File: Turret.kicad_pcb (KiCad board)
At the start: 2 copper layers, 104 x 54 mm, 25 parts, among them J1 Conn_01x04_Pin, J10 Conn_01x02_Pin, J12 Conn_01x02_Pin, J13 Conn_01x04_Pin, J14 Conn_01x04_Pin, J15 Conn_01x08_Pin, J2 Conn_01x02_Pin, J20 Conn_01x02_Pin, J21 Conn_01x02_Pin, J3 Conn_01x02_Pin, J4 Conn_01x02_Pin, J5 Conn_01x04_Pin, J6 Conn_01x02_Pin, J7 Conn_01x02_Pin, J8 Conn_01x02_Pin, J9 Conn_01x02_Pin

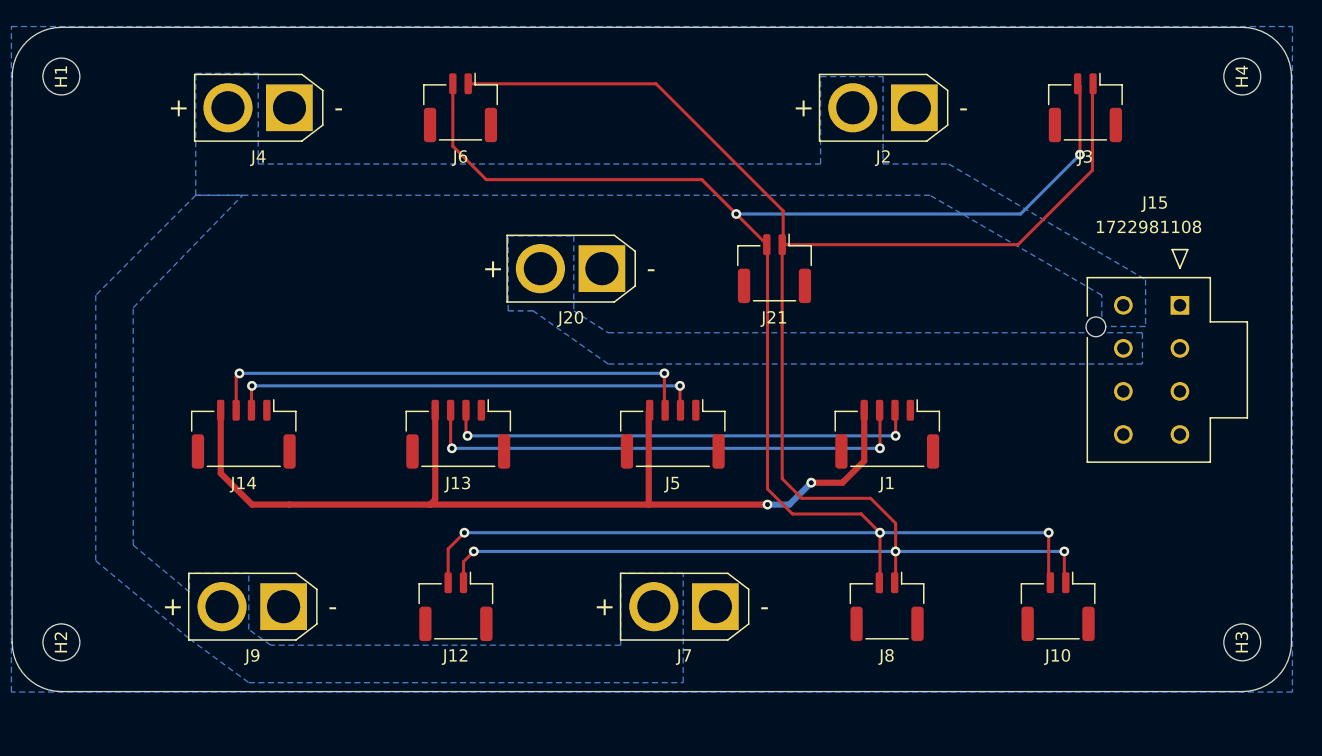
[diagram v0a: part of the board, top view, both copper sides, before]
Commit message: Adding new ref system, other push now deprecated
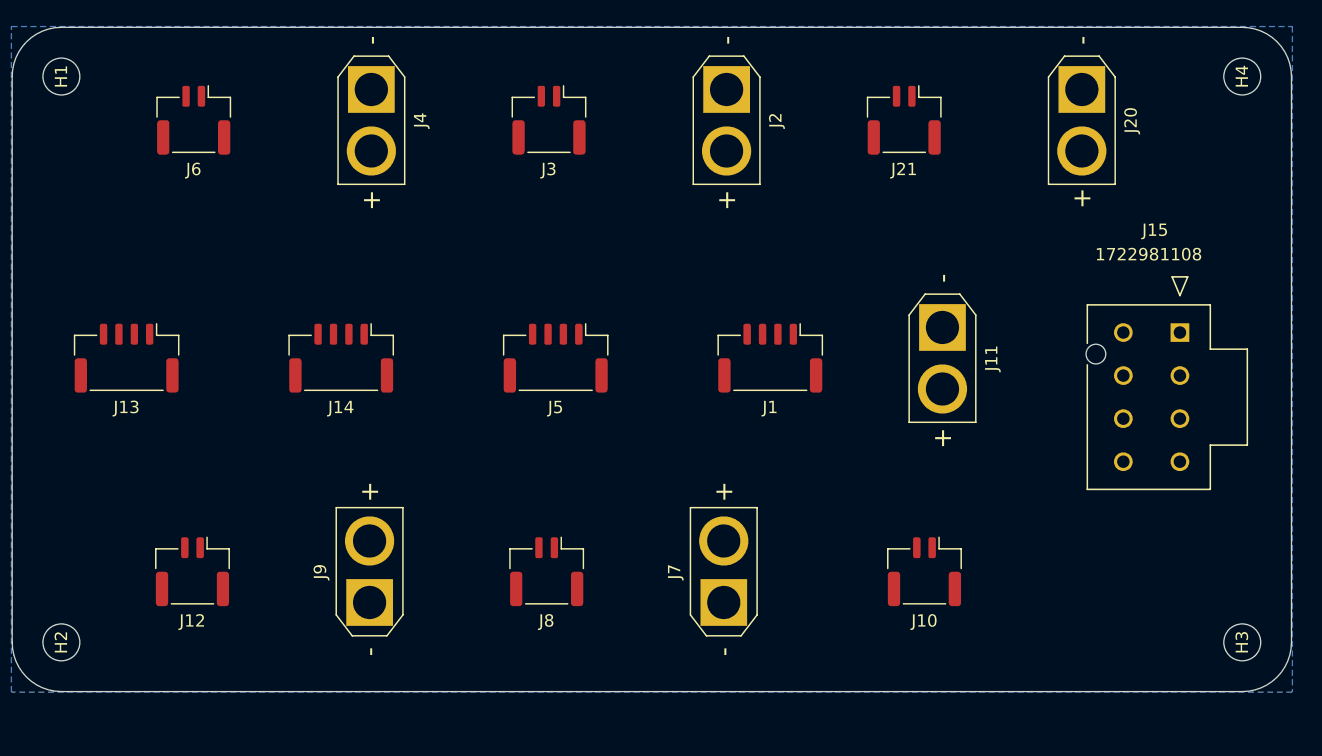
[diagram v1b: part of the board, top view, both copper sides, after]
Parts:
- added J11: Conn_01x02_Pin, Connector_AMASS:AMASS_XT30U-F_1x02_P5.0mm_Vertical, F.Cu at (116.1, 58.5)
- moved J3 43.6 mm to (84.1, 41.7)
- moved J20 41.6 mm to (127.4, 39.2), turned to -90 degrees
- moved J8 27.8 mm to (83.9, 78.4)
- moved J13 27.7 mm to (49.8, 61.0)
- moved J6 21.7 mm to (55.2, 41.7)
- moved J12 21.6 mm to (55.1, 78.4)
- moved J21 16.0 mm to (113.0, 41.7)
- moved J2 15.3 mm to (98.5, 39.2), turned to -90 degrees
- moved J5 11.3 mm to (84.6, 61.0)
- moved J1 11.3 mm to (102.1, 61.0)
- moved J10 11.2 mm to (114.6, 78.4)
- moved J14 10.0 mm to (67.2, 61.0)
- moved J9 7.00 mm to (69.5, 80.9), turned to 90 degrees
- moved J4 6.82 mm to (69.6, 39.2), turned to -90 degrees
- moved J15 2.21 mm to (135.4, 58.9)
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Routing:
- net /CANH: track 160.5 -> 0.00 mm, vias 5 -> 0
- net /CANL: track 155.5 -> 0.00 mm, vias 3 -> 0
- net +3.3V: track 79.6 -> 0.00 mm, vias 2 -> 0
- net /UART_RX: track 41.0 -> 0.00 mm, vias 2 -> 0
- net /SWCLK: track 40.7 -> 0.00 mm, vias 2 -> 0
- net /UART_TX: track 39.0 -> 0.00 mm, vias 2 -> 0
- net /SWDIO: track 38.8 -> 0.00 mm, vias 2 -> 0
- removed copper zone on B.Cu, net /+24V_Gimbal
- removed copper zone on B.Cu, net /+24V_Shooter

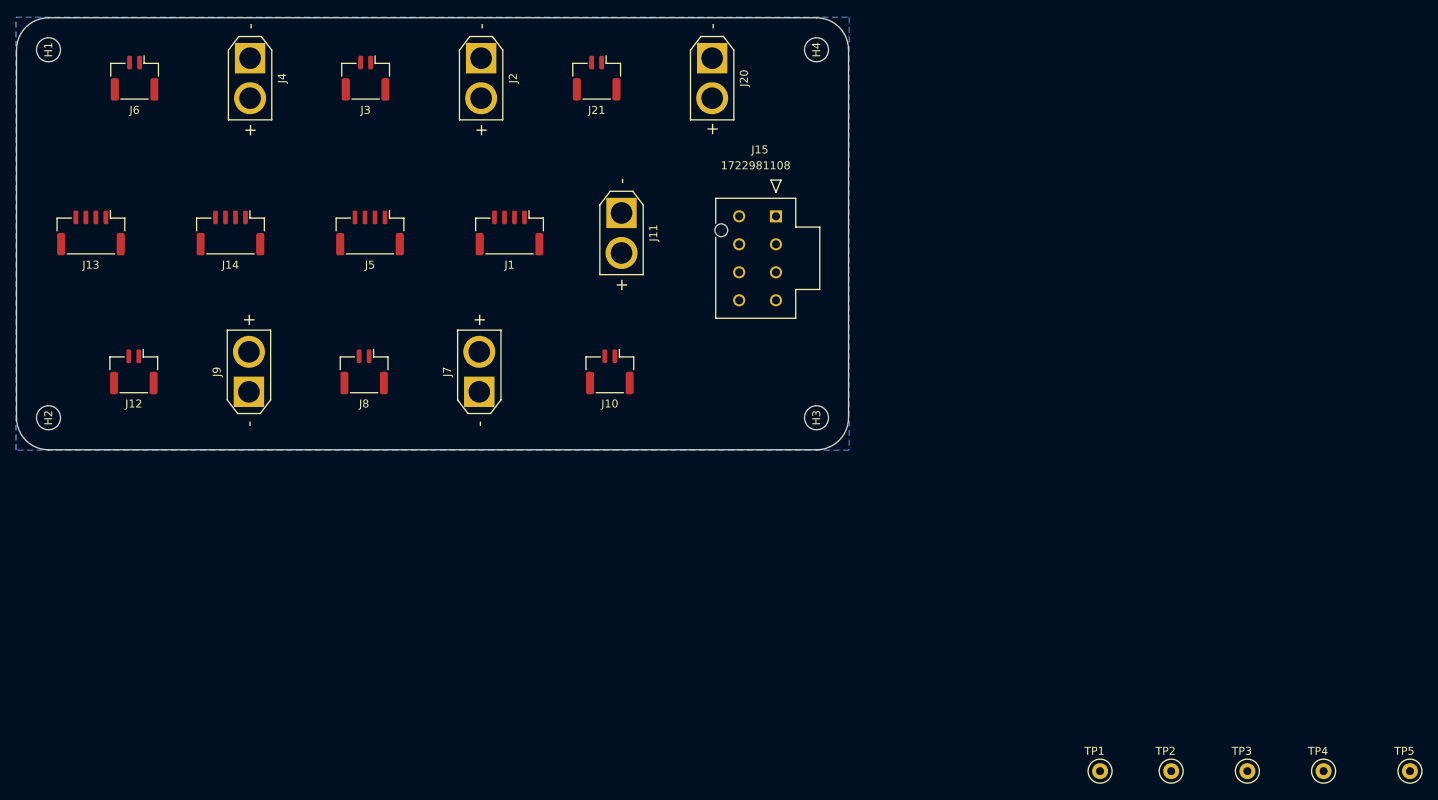
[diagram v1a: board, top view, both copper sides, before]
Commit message: New layout, test points not final
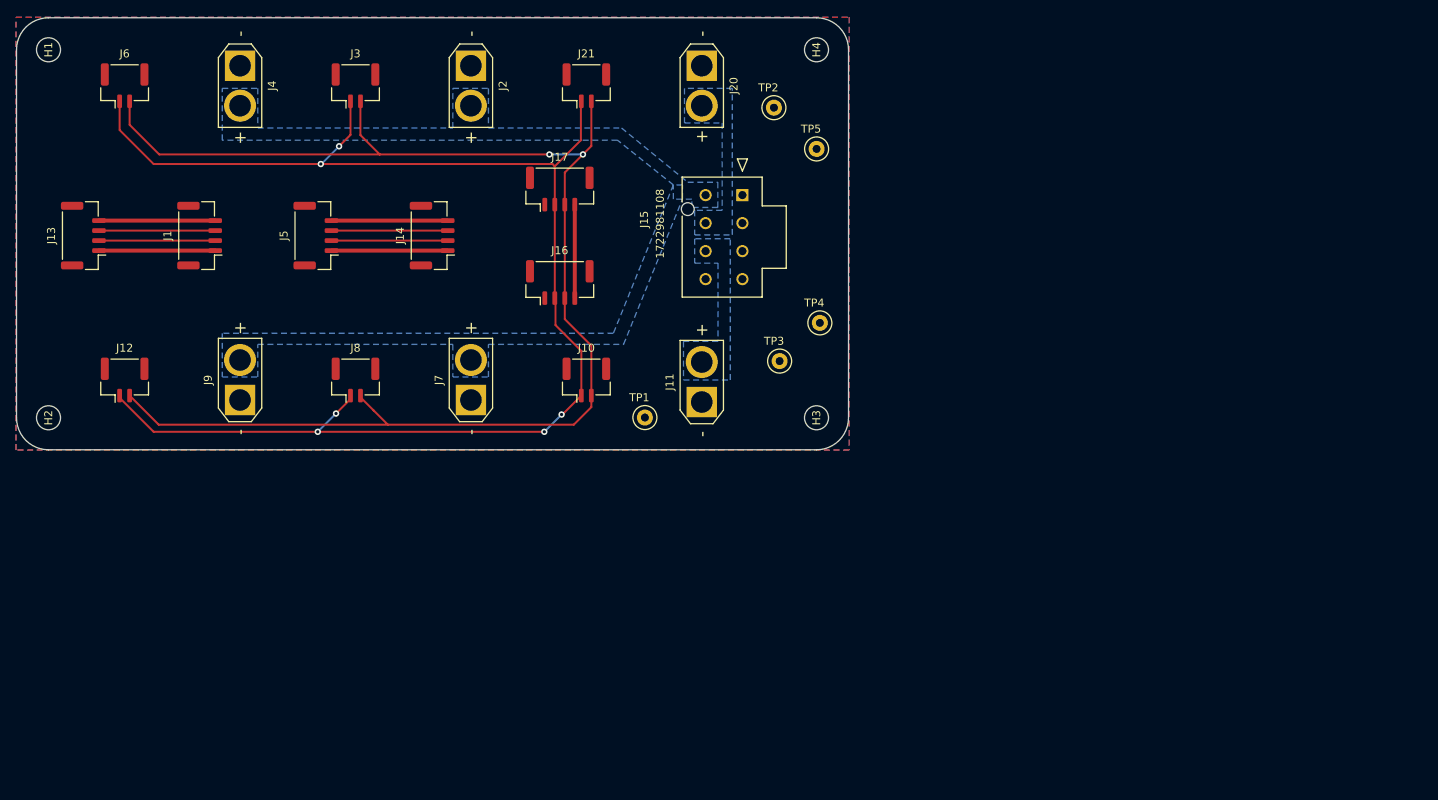
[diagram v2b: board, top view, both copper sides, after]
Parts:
- added J16: Conn_01x04_Pin, Connector_JST:JST_GH_BM04B-GHS-TBT_1x04-1MP_P1.25mm_Vertical, F.Cu at (108.4, 67.2)
- added J17: Conn_01x04_Pin, Connector_JST:JST_GH_BM04B-GHS-TBT_1x04-1MP_P1.25mm_Vertical, F.Cu at (108.4, 55.5)
- moved TP5 107.5 mm to (140.5, 50.5)
- moved TP2 96.7 mm to (135.1, 45.3)
- moved TP4 84.3 mm to (140.9, 72.2)
- moved TP3 77.8 mm to (135.8, 77.0)
- moved TP1 72.0 mm to (119.0, 84.1)
- moved J1 38.7 mm to (63.3, 61.3), turned to 90 degrees
- moved J11 25.7 mm to (126.1, 82.1), turned to 90 degrees
- moved J14 25.2 mm to (92.4, 61.3), turned to 90 degrees
- moved J5 6.77 mm to (77.9, 61.3), turned to 90 degrees
- moved J15 4.96 mm to (131.2, 56.3)
- moved J10 3.11 mm to (111.7, 79.4), turned to 0 degrees
- moved J20 1.60 mm to (126.1, 40.1)
- moved J21 1.59 mm to (111.7, 42.6), turned to 0 degrees
- moved J2 1.58 mm to (97.3, 40.1)
- moved J3 1.58 mm to (82.8, 42.6), turned to 0 degrees
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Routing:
- net /CANL: track 0.00 -> 176.7 mm, vias 0 -> 6
- net /CANH: track 0.00 -> 174.9 mm, vias 0 -> 2
- net GND: track 0.00 -> 29.1 mm
- net +3.3V: track 0.00 -> 29.1 mm
- net /UART_TX: track 0.00 -> 14.5 mm
- net /UART_RX: track 0.00 -> 14.5 mm
- net /SWDIO: track 0.00 -> 14.5 mm
- net /SWCLK: track 0.00 -> 14.5 mm
- net /Ref_PWR: track 0.00 -> 11.7 mm
- added copper zone on B.Cu, net /+19V
- added copper zone on B.Cu, net /+24V_Gimbal
- added copper zone on B.Cu, net /+24V_Shooter
- added copper zone on F.Cu, net GND

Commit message: Added connections to test points, silkscreens need to be renamed.
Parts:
- moved TP3 7.41 mm to (134.0, 84.2)
- moved TP2 7.33 mm to (134.0, 38.1)
- moved TP4 0.43 mm to (140.4, 72.3)
- moved TP5 0.15 mm to (140.4, 50.3)
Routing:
- net /+5V: track 0.00 -> 16.2 mm
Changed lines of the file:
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@@
   )
   (footprint "TestPoint:TestPoint_Loop_D1.80mm_Drill1.0mm_Beaded" (layer "F.Cu")
-    (at 135.128 45.339 180)
+    (at 133.9596 38.1 180)
     (descr "wire loop with bead as test point, loop diameter 1.8mm, hole diameter 1.0mm")
     (tags "test point wire loop bead")
@@
   )
   (footprint "TestPoint:TestPoint_Loop_D1.80mm_Drill1.0mm_Beaded" (layer "F.Cu")
-    (at 135.8392 77.0128 180)
+    (at 133.9596 84.1756 180)
     (descr "wire loop with bead as test point, loop diameter 1.8mm, hole diameter 1.0mm")
     (tags "test point wire loop bead")
@@
   )
   (footprint "TestPoint:TestPoint_Loop_D1.80mm_Drill1.0mm_Beaded" (layer "F.Cu")
-    (at 140.8684 72.2376 180)
+    (at 140.45 72.3392 180)
     (descr "wire loop with bead as test point, loop diameter 1.8mm, hole diameter 1.0mm")
     (tags "test point wire loop bead")
@@
   )
   (footprint "TestPoint:TestPoint_Loop_D1.80mm_Drill1.0mm_Beaded" (layer "F.Cu")
-    (at 140.462 50.4952 180)
+    (at 140.45 50.3428 180)
     (descr "wire loop with bead as test point, loop diameter 1.8mm, hole diameter 1.0mm")
     (tags "test point wire loop bead")
@@
   (segment (start 79.820334 61.953) (end 94.354167 61.953) (width 0.25) (layer "F.Cu") (net 7))
   (segment (start 79.820334 60.703) (end 94.354167 60.703) (width 0.25) (layer "F.Cu") (net 8))
+  (segment (start 126.587999 66.766002) (end 132.161197 72.3392) (width 0.25) (layer "F.Cu") (net 12))
+  (segment (start 132.161197 72.3392) (end 140.45 72.3392) (width 0.25) (layer "F.Cu") (net 12))
   (segment (start 110.233 57.457) (end 110.233 69.141) (width 0.5) (layer "F.Cu") (net 13))
   (zone (net 3) (net_name "GND") (layer "F.Cu") (hatch edge 0.5)
@@
       (pts
         (xy 128.1176 54.6608)
-        (xy 128.1176 57.8104)
-        (xy 124.8664 57.8104)
+        (xy 128.1176 57.6326)
+        (xy 124.8664 57.6326)
         (xy 124.8664 56.769)
         (xy 122.555 56.769)
@@
     )
   )
+  (zone (net 10) (net_name "/+24V_Gimbal") (layer "B.Cu") (hatch edge 0.5)
+    (priority 7)
+    (connect_pads (clearance 0.5))
+    (min_thickness 0.25) (filled_areas_thickness no)
+    (fill yes (thermal_gap 0.5) (thermal_bridge_width 0.5))
+    (polygon
+      (pts
+        (xy 129.921 43.5102)
+        (xy 129.921 42.926)
+        (xy 129.3876 42.926)
+        (xy 132.1308 39.3954)
+        (xy 132.1308 36.2458)
+        (xy 135.7884 36.2712)
+        (xy 135.7884 39.9288)
+        (xy 132.6388 39.9288)
+      )
+    )
+  )
+  (zone (net 11) (net_name "/+19V") (layer "B.Cu") (hatch edge 0.5)
+    (priority 6)
+    (connect_pads (clearance 0.5))
+    (min_thickness 0.25) (filled_areas_thickness no)
+    (fill yes (thermal_gap 0.5) (thermal_bridge_width 0.5))
+    (polygon
+      (pts
+        (xy 129.667 79.375)
+        (xy 132.1308 82.3976)
+        (xy 132.1308 86.0044)
+        (xy 135.7892 86.0044)
+        (xy 135.7892 82.3484)
+        (xy 133.05 82.3484)
+        (xy 129.667 78.2)
+      )
+    )
+  )
+  (zone (net 9) (net_name "/+24V_Shooter") (layer "B.Cu") (hatch edge 0.5)
+    (priority 5)
+    (connect_pads (clearance 0.5))
+    (min_thickness 0.25) (filled_areas_thickness no)
+    (fill yes (thermal_gap 0.5) (thermal_bridge_width 0.5))
+    (polygon
+      (pts
+        (xy 116.8146 73.7362)
+        (xy 116.332 74.93)
+        (xy 118.364 80.518)
+        (xy 118.364 82.2452)
+        (xy 117.1448 82.2452)
+        (xy 117.1956 85.9028)
+        (xy 120.8532 85.9028)
+        (xy 120.8532 82.2452)
+        (xy 119.2022 82.2452)
+        (xy 119.2022 80.518)
+      )
+    )
+  )
   (zone (net 11) (net_name "/+19V") (layer "B.Cu") (hatch edge 0.5)
     (priority 1)
@@
         (xy 123.825 74.549)
         (xy 123.825 79.375)
-        (xy 129.667 79.375)
-        (xy 129.667 61.722)
+        (xy 129.921 79.375)
+        (xy 129.921 61.722)
       )
     )

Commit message: Tried to fix footprints, also changed to traces for testpoints
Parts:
- +19V_Turret->Orin1: renamed from J11; footprint Connector_AMASS:AMASS_XT30U-F_1x02_P5.0mm_Vertical -> Robomaster_ICs:AMASS_XT30U-F_1x02_P5.0mm_Vertical_copy
- +24V_Feeder1: renamed from J7; footprint Connector_AMASS:AMASS_XT30U-F_1x02_P5.0mm_Vertical -> Robomaster_ICs:AMASS_XT30U-F_1x02_P5.0mm_Vertical_copy
- +24V_Gimbal1: renamed from J20; footprint Connector_AMASS:AMASS_XT30U-F_1x02_P5.0mm_Vertical -> Robomaster_ICs:AMASS_XT30U-F_1x02_P5.0mm_Vertical_copy
- +24V_L_Flywheel1: renamed from J2; footprint Connector_AMASS:AMASS_XT30U-F_1x02_P5.0mm_Vertical -> Robomaster_ICs:AMASS_XT30U-F_1x02_P5.0mm_Vertical_copy
- +24V_R_Flywheel1: renamed from J4; footprint Connector_AMASS:AMASS_XT30U-F_1x02_P5.0mm_Vertical -> Robomaster_ICs:AMASS_XT30U-F_1x02_P5.0mm_Vertical_copy
- +24V_Waterwheel1: renamed from J9; footprint Connector_AMASS:AMASS_XT30U-F_1x02_P5.0mm_Vertical -> Robomaster_ICs:AMASS_XT30U-F_1x02_P5.0mm_Vertical_copy
- renumbered TP3 to +19V1, TP2 to +24V_Gimbal2, TP1 to +24V_Shooter2, TP4 to +5V1, J15 to 8_Pin_Slipring->Turret1, J8 to CAN_Feeder1, J21 to CAN_Gimbal1, J10 to CAN_In1, J3 to CAN_L_Flywheel1, J6 to CAN_R_Flywheel1, J12 to CAN_Waterwheel1, J14 to Debug_Orin->Turret1, J5 to Debug_Turret->Chassis1, TP5 to GND1, J16 to Ref_In1, J17 to Ref_Out1, J1 to UART_Chassis->Turret1, J13 to UART_Turret->Orin1
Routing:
- net +3.3V: track 29.1 -> 43.6 mm
- net /+19V: track 0.00 -> 10.8 mm
- net /+24V_Gimbal: track 0.00 -> 10.7 mm
